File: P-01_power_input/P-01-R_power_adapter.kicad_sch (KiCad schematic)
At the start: 14 parts, among them J1 POWER_A, J2 POWER_B, J3 CHAIN_TOP, J4 +5V_OUT, J5 POWER_IN, J6 CHAIN_BOTTOM

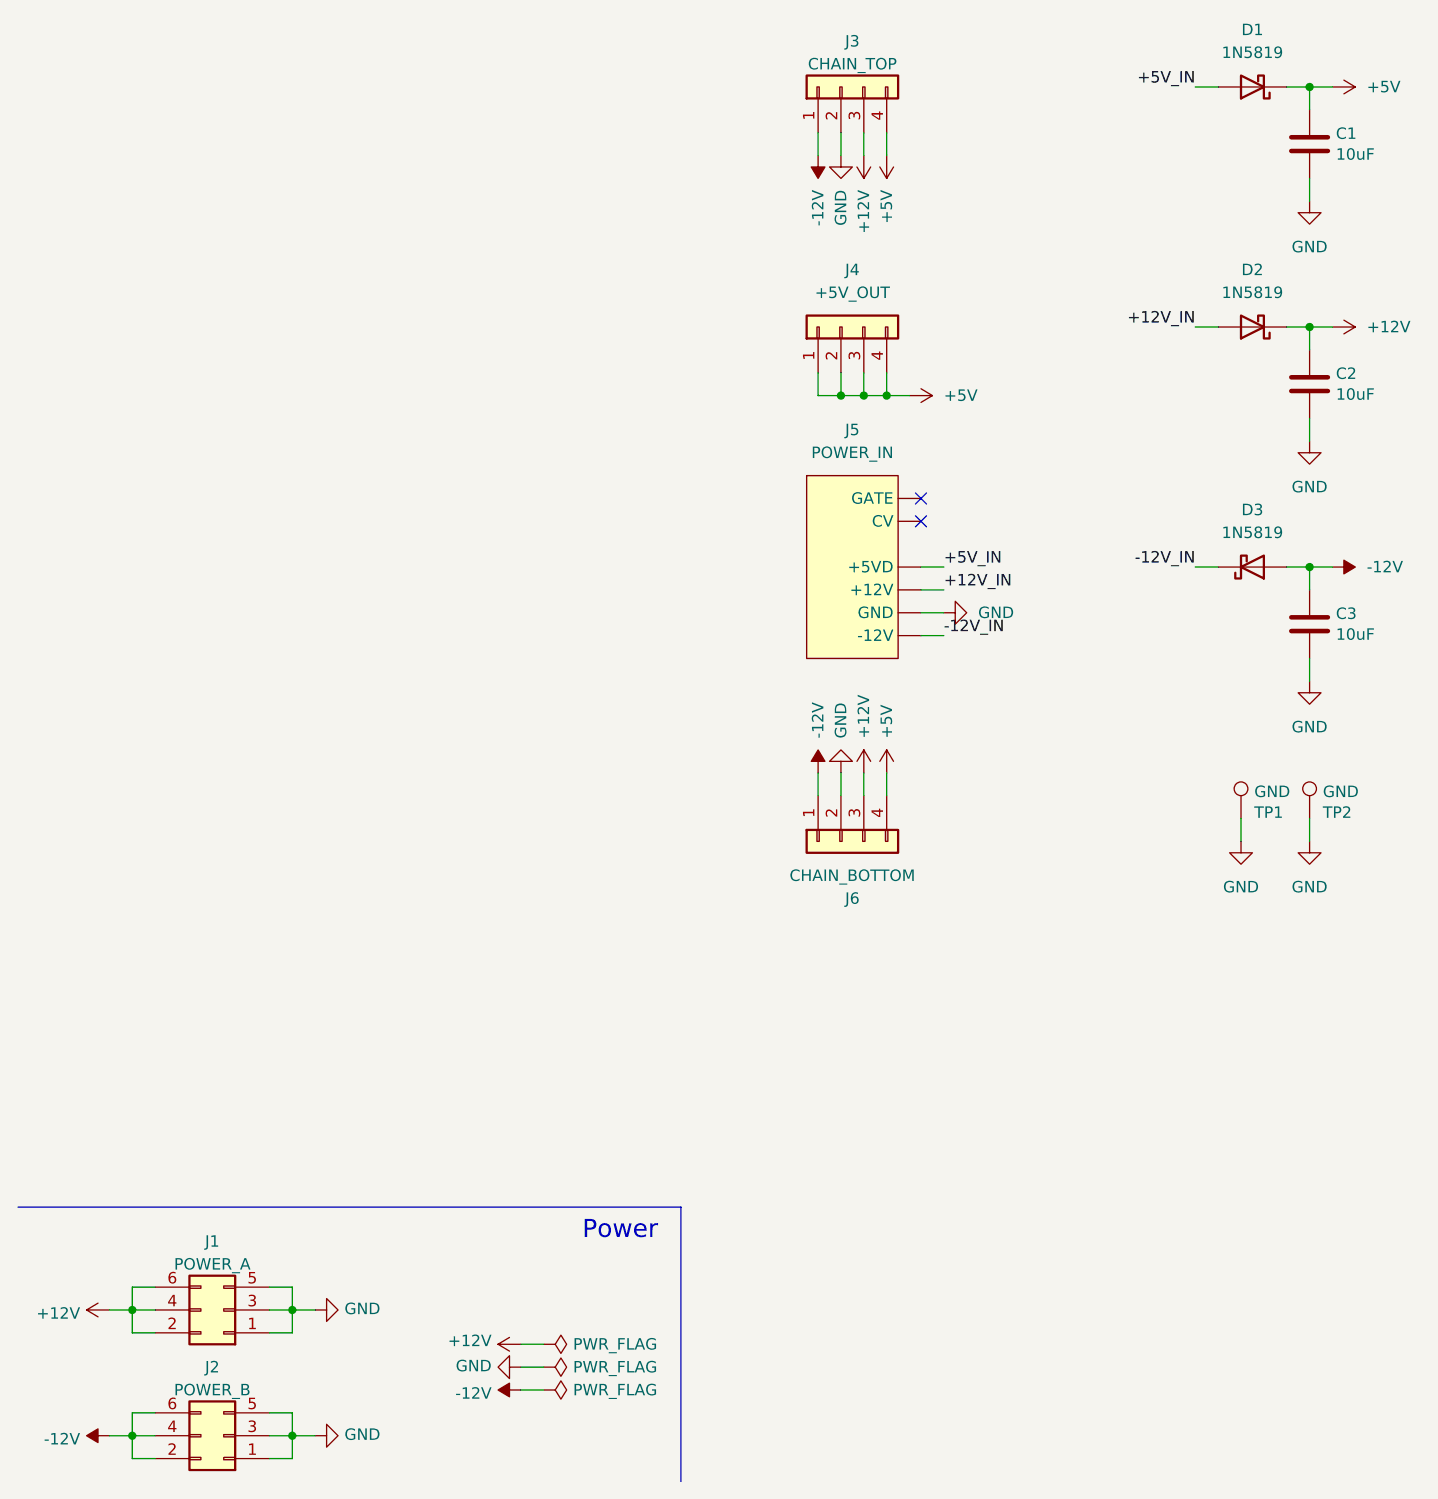
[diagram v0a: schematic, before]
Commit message: Fix P-01 file associations, diodes, erc check
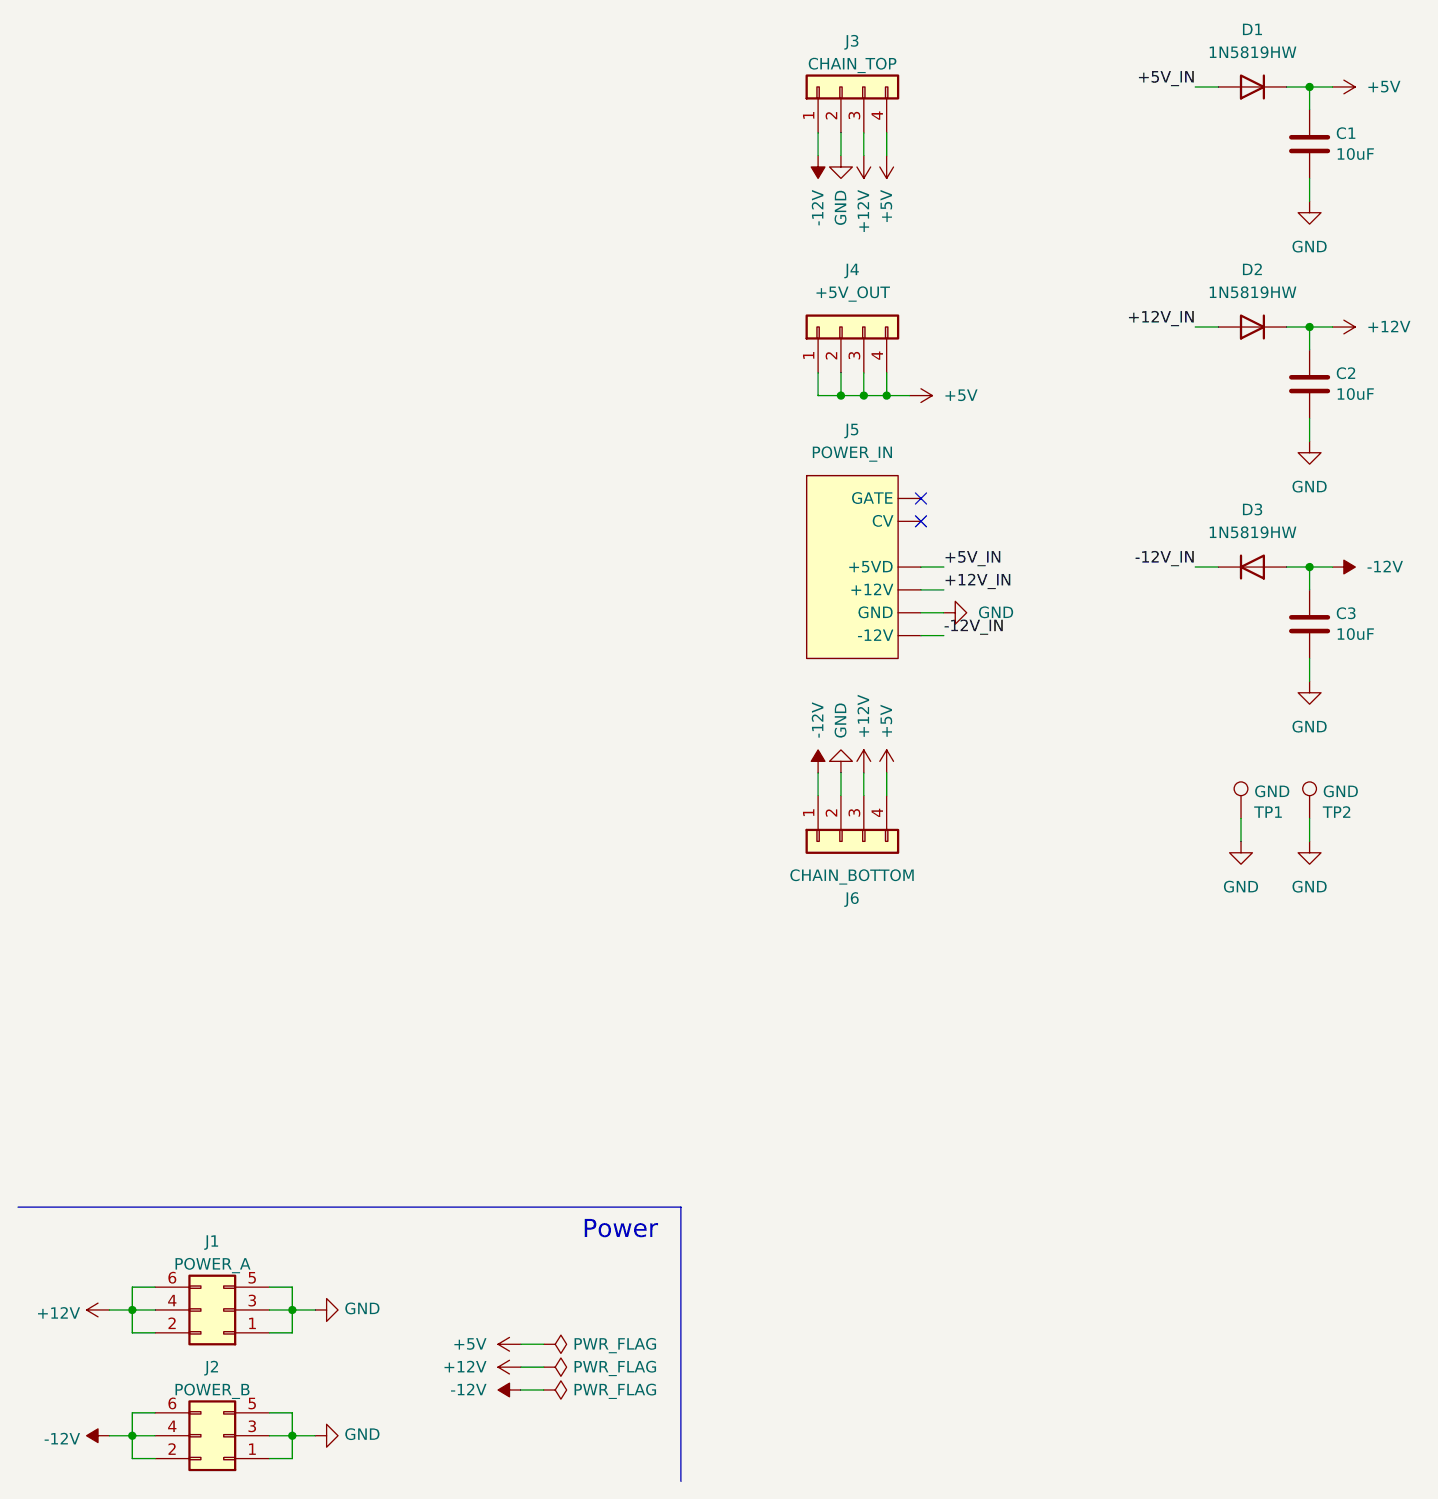
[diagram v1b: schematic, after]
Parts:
- D1, D2, D3: value 1N5819 -> 1N5819HW; symbol Diode:1N5819 -> Device:D
